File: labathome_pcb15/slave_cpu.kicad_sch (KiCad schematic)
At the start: 34 parts, among them J1 HALL, J27 ADDA, J28 ???, J31 Servo1, J32 Servo2, J33 Servo3, U3 DRV8813, U5 STM32G431C6Ux, Y1 8MHz

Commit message: labathome wip
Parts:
- added J26: Conn_01x06, Connector_PinHeader_2.54mm:PinHeader_1x06_P2.54mm_Vertical, symbol Connector_Generic:Conn_01x06
- J28: value ??? -> Brushless
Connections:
- net ADC2_IN12 is gone; now on net BRIGHTNESS: U5.19 (PB2)
- net BOOT0 is gone; now on net BTN_RED: U5.46 (PB8)
- net BTN_GRN is gone; now on net HEATER: U5.16 (PC4)
- net T15.1_ADC1.5 is gone; now on net ADC_IN1: U5.27 (PB14)
- net T15.2_ADC2.15 is gone; now on net ADC_IN2: U5.28 (PB15)
- net T2.4 is gone; now on net Relais: U5.24 (PB11)
- net +3V3: now also J26.6 (Pin_6)
- net BL_FAULT: now also U5.26 (PB13)
- net BL_RESET: now also U5.25 (PB12)
- net BRIGHTNESS: no longer U5.25 (PB12)
- net BTN_RED: no longer U5.3 (PC14)
- net BTN_YEL: now also U5.2 (PC13); no longer U5.4 (PC15)
- net GND: now also J26.1 (Pin_1)
- net HEATER: no longer U5.10 (PA2)
- net MOVE: now also U5.3 (PC14); no longer U5.2 (PC13)
- net Relais: no longer U5.26 (PB13)
- net Servo1: now also U5.10 (PA2); no longer U5.11 (PA3)
- net Servo2: now also U5.11 (PA3)
- net Servo3: now also U5.14 (PA6)
- net UART4_RX: now also J26.5 (Pin_5)
- net UART4_TX: now also J26.4 (Pin_4)
- net STM32_RESET: now reaches U5.7 (PG10)
- net ADC2_IN3 renamed ADC_IN1
- net ADC_IN1: no longer U5.14 (PA6)
- net ADC2_IN4 renamed ADC_IN2
- net ADC_IN2: no longer U5.15 (PA7)
- net BL_IN1 renamed BL_DRV1
- net BL_IN2 renamed BL_DRV2
- net BL_IN3 renamed BL_DRV3
- net GPIO_PB3: no longer names the net of U5.41 (PB3)
- net JTCK renamed SWCLK
- net SWCLK: now also J26.3 (Pin_3)
- net JTMS renamed SWDIO
- net SWDIO: now also J26.2 (Pin_2)
- net T2.3: no longer names the net of U5.22 (PB10)
- new net FAN2_DRIVE: U5.15 (PA7)
- new net PC15: U5.4 (PC15)
- no-connect marks 1 -> 3
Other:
- note added: "ADC2.12"
- note added: "I2C1.D T4.2 T3.4"
- note added: "I2C3.D"
- note added: "Input"
- note added: "PROG"
- note added: "Slow Software-PWM!"
- note added: "T1.1 I2C2.D"
- note added: "T1.2 I2C2.C T2.3 CC1"
- note added: "T1.3 T2.4 CC2"
- note added: "T16.1 T4.3 T8.2 Boot0"
- note added: "T2.1 ADC12.1"
- note added: "T2.1 T8.1 I2C1.C"
- note added: "T2.2"
- note added: "T2.2 ADC12.2"
- note added: "T2.3"
- note added: "T2.3 T15.1"
- note added: "T2.4 T15.2"
- note added: "T3.1 T8.1"
- note added: "T3.2 I2C3.D"
- note added: "T3.4 ADC1.12"
- note added: "T4.4"
- note removed: "BL_ENABLE?"
- note removed: "T1.1"
- note removed: "T1.2"
- note removed: "T1.3"
- note removed: "T2.1 T8.1"
- note removed: "T2.3_T15.1"
- note removed: "T2.4_T15.2"
- note removed: "T3.2"
- note removed: "T3.4"
- note removed: "TIM2.1"
- note removed: "TIM2.2"
- note removed: "TIM4.4"
- note removed: "TIM8.1"
- note removed: "Taster1?"
- note removed: "Taster2?"
- note removed: "i2c=I2C1"
- moved on the sheet: R49, R63, Y1

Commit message: labathome15 v0.0.1
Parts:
- J26: value Conn_01x06 -> G D C T R 3
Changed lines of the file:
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@@
 			)
 		)
-		(property "Value" "Conn_01x06"
+		(property "Value" "G D C T R 3"
 			(at 46.99 99.0599 0)
 			(effects

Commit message: labathome_pcb15 v0.0.2
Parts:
- removed J26: G D C T R 3, Connector_PinHeader_2.54mm:PinHeader_1x06_P2.54mm_Vertical, symbol Connector_Generic:Conn_01x06
- added C50, C61: 22p, Capacitor_SMD:C_0402_1005Metric, symbol Device:C
- added J25: STM Debug, liebler_CONN:JST_SH_BM06B-SRSS-TB_1x06-1MP_P1.00mm_Vertical_handsolder, symbol Connector_Generic:Conn_01x06
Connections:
- net +3V3: now also J25.1 (Pin_1)
- net GND: now also C50.1, C61.1, J25.6 (Pin_6)
- net SWCLK: now also J25.3 (Pin_3)
- net SWDIO: now also J25.2 (Pin_2)
- net UART4_RX: now also J25.5 (Pin_5)
- net UART4_TX: now also J25.4 (Pin_4)
- net at R49.2, Y1.1: now also C50.2
- net at U5.5 (PF0), Y1.3: now also C61.2
- net PC15: no longer names the net of U5.4 (PC15)
- no-connect marks 3 -> 7

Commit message: labathome_pcb15 ready for first review
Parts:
- added D19: INFO, LED_SMD:LED_0805_2012Metric, symbol Device:LED
- added R34: k22, Resistor_SMD:R_0402_1005Metric, symbol Device:R
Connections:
- net GND: now also R34.1
- net LED_INFO: now reaches U5.41 (PB3)
- net LED_INFO: now also D19.2 (A)
- new net: D19.1 (K), R34.2
- no-connect marks 7 -> 4
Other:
- moved on the sheet: J25

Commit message: labathome_pcb15
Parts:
- C32, C33, C34, C35: value u1 -> u1
- C38: value u1 -> 10n/35V; footprint Capacitor_SMD:C_0603_1608Metric -> Capacitor_SMD:C_0402_1005Metric
- C49: value 10n -> u1
- C50, C61: value 22p -> 15p
- C51: value u1 -> u1/16V; footprint Capacitor_SMD:C_0603_1608Metric -> Capacitor_SMD:C_0402_1005Metric
- D19: footprint LED_SMD:LED_0805_2012Metric -> LED_SMD:LED_0805_2012Metric_Pad1.15x1.40mm_HandSolder
- U3: value DRV8813 -> DRV8313
- Y1: value 8MHz -> 8MHz/12pF
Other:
- note added: "Annahme Streukapaität 5pF Lastkapazität = (12pF-5pF)*2=15pF"
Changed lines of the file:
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@@
 		)
 	)
+	(text "Annahme Streukapaität 5pF \nLastkapazität = (12pF-5pF)*2=15pF"
+		(exclude_from_sim no)
+		(at 64.77 61.214 0)
+		(effects
+			(font
+				(size 1.27 1.27)
+			)
+		)
+	)
 	(text "T3.3 ADC1.15"
 		(exclude_from_sim no)
@@
 		(on_board yes)
 		(dnp no)
-		(fields_autoplaced yes)
 		(property "Reference" "Y1"
-			(at 93.98 48.2914 0)
+			(at 96.52 48.2914 0)
 			(effects
 				(font
@@
 			)
 		)
-		(property "Value" "8MHz"
-			(at 93.98 50.8314 0)
+		(property "Value" "8MHz/12pF"
+			(at 94.234 45.72 0)
 			(effects
 				(font
@@
 			)
 		)
-		(property "Value" "u1	"
+		(property "Value" "u1"
 			(at 100.33 35.052 0)
 			(effects
@@
 			)
 		)
-		(property "Value" "22p"
+		(property "Value" "15p"
 			(at 77.47 52.832 0)
 			(effects
@@
 			)
 		)
-		(property "Value" "u1	"
+		(property "Value" "u1"
 			(at 95.25 35.052 0)
 			(effects
@@
 			)
 		)
-		(property "Value" "DRV8813"
+		(property "Value" "DRV8313"
 			(at 243.84 46.99 0)
 			(effects
@@
 			)
 		)
-		(property "Value" "u1	"
+		(property "Value" "u1/16V"
 			(at 264.16 59.182 0)
 			(effects
@@
 			)
 		)
-		(property "Footprint" "Capacitor_SMD:C_0603_1608Metric"
+		(property "Footprint" "Capacitor_SMD:C_0402_1005Metric"
 			(at 267.6652 60.96 0)
 			(effects
@@
 			)
 		)
-		(property "Value" "u1	"
+		(property "Value" "u1"
 			(at 110.49 35.052 0)
 			(effects
@@
 			)
 		)
-		(property "Value" "22p"
+		(property "Value" "15p"
 			(at 96.52 52.832 0)
 			(effects
@@
 			)
 		)
-		(property "Footprint" "LED_SMD:LED_0805_2012Metric"
+		(property "Footprint" "LED_SMD:LED_0805_2012Metric_Pad1.15x1.40mm_HandSolder"
 			(at 163.83 97.79 0)
 			(effects
@@
 			)
 		)
-		(property "Value" "u1	"
+		(property "Value" "u1"
 			(at 105.41 35.052 0)
 			(effects
@@
 			)
 		)
-		(property "Value" "u1	"
+		(property "Value" "10n/35V"
 			(at 256.54 54.102 0)
 			(effects
@@
 			)
 		)
-		(property "Footprint" "Capacitor_SMD:C_0603_1608Metric"
+		(property "Footprint" "Capacitor_SMD:C_0402_1005Metric"
 			(at 260.0452 55.88 0)
 			(effects
@@
 			)
 		)
-		(property "Value" "10n"
+		(property "Value" "u1"
 			(at 149.86 28.702 0)
 			(effects

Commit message: labathome_pcb5 ready for review, 2nd
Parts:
- removed J25: STM Debug, liebler_CONN:JST_SH_BM06B-SRSS-TB_1x06-1MP_P1.00mm_Vertical_handsolder, symbol Connector_Generic:Conn_01x06
- added J26: STDC14, liebler_CONN:IDC_2x07_P1.27mm_Vertical, symbol Connector_Generic:Conn_02x07_Odd_Even
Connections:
- net +3V3: now also D19.2 (A), J26.3 (Pin_3)
- net GND: now also J26.11 (Pin_11), J26.2 (Pin_2), J26.5 (Pin_5), J26.7 (Pin_7); no longer R34.1
- net LED_INFO: now also R34.1; no longer D19.2 (A)
- net SWCLK: now also J26.6 (Pin_6)
- net SWDIO: now also J26.4 (Pin_4)
- net UART4_RX: now also J26.13 (Pin_13)
- net UART4_TX: now also J26.14 (Pin_14)
- no-connect marks 4 -> 9
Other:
- note removed: "PROG"

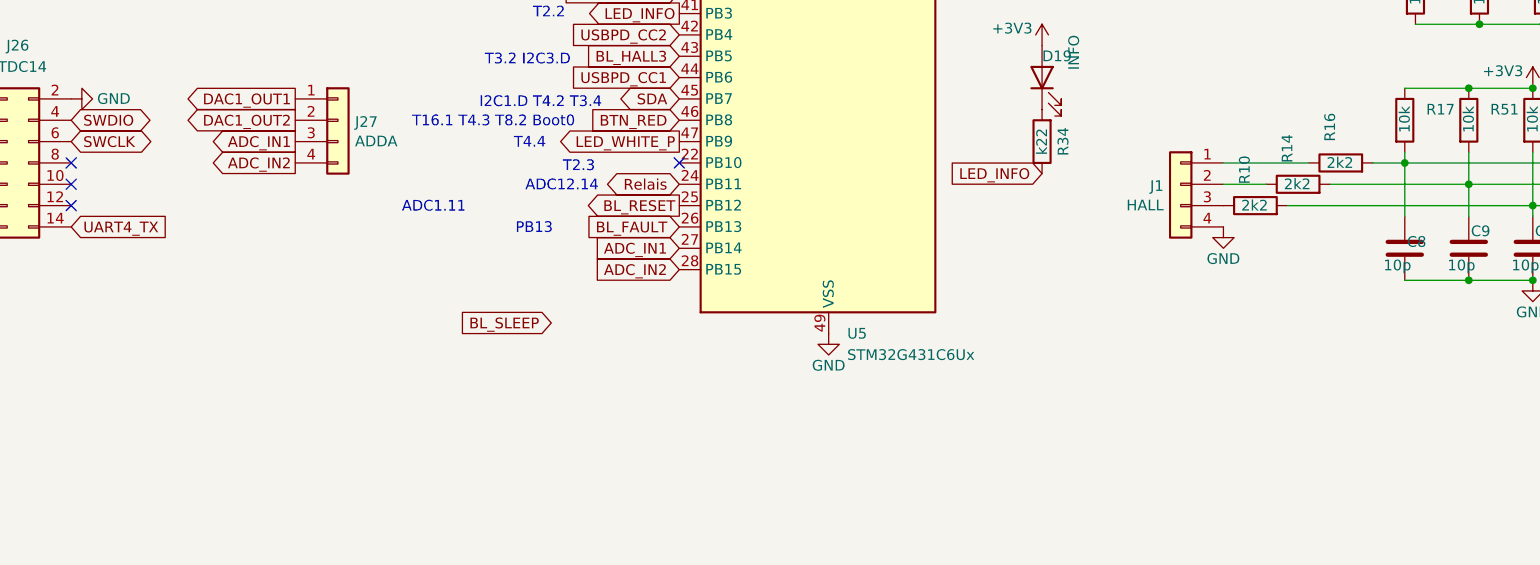
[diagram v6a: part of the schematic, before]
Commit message: Various PCB and Code updates after review from Jana Marie Hemsing. Big Thankyou
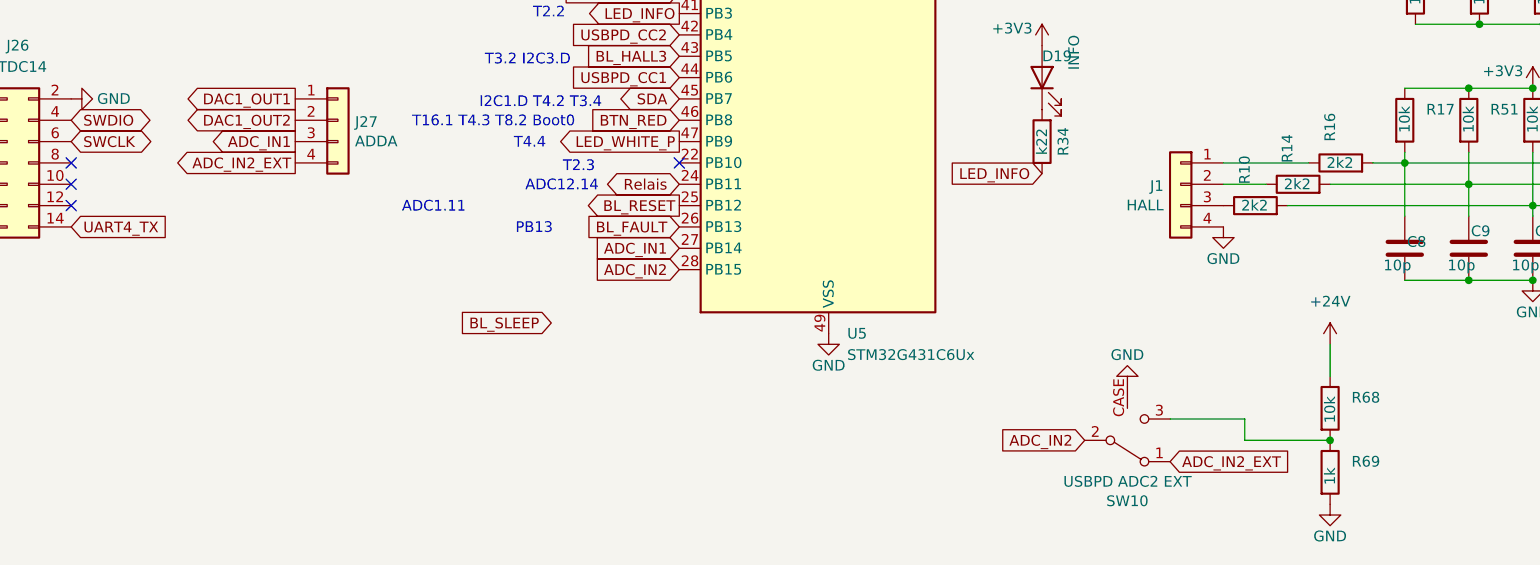
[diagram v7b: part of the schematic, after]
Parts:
- added R68: 10k, Resistor_SMD:R_0402_1005Metric, symbol Device:R
- added R69: 1k, Resistor_SMD:R_0402_1005Metric, symbol Device:R
- added SW10: USBPD ADC2 EXT, liebler_MECH:SW_SPDT_PCM12_handsolder, symbol liebler_MECH:SW_SPDT_with_Case
- J26: footprint liebler_CONN:IDC_2x07_P1.27mm_Vertical -> Connector_IDC:IDC-Header_2x07_P2.54mm_Vertical
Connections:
- net +24V: now also R68.1
- net ADC_IN2: now also SW10.2 (B); no longer J27.4 (Pin_4)
- net GND: now also R69.2, SW10.CASE
- new net: R68.2, R69.1, SW10.3 (C)
- new net ADC_IN2_EXT: J27.4 (Pin_4), SW10.1 (A)

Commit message: Further improventents in PCB layout
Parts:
- added C25: u1/16V, Capacitor_SMD:C_0402_1005Metric, symbol Device:C
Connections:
- net GND: now also C25.2
- net STM32_RESET: now also C25.1
- no-connect marks 9 -> 8
